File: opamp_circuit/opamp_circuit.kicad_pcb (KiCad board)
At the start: 2 copper layers, 49 parts, among them J1 INP, J2 INM, J3 Vout, J4 VDD, J5 VSS, J6 Vref, J7 Vref_out, J8 GND, U1 OPA846xDBV, U2 OPA846xDBV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

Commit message: Version Vicente before advices
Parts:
- moved C22 89.8 mm to (62.7, 67.9)
- moved C20 89.6 mm to (62.7, 71.7)
- moved C21 88.7 mm to (62.7, 70.2)
- moved J3 87.7 mm to (75.2, 63.0)
- moved R9 86.6 mm to (66.2, 63.1)
- moved U3 85.1 mm to (57.5, 63.7)
- moved C27 79.9 mm to (55.6, 71.8)
- moved Rg1 79.6 mm to (51.3, 63.8)
- moved C26 79.5 mm to (55.6, 70.4)
- moved C23 79.3 mm to (60.4, 54.9)
- moved C25 78.6 mm to (61.2, 59.1)
- moved C24 78.3 mm to (60.6, 56.8)
- moved R6 77.4 mm to (55.6, 68.7), turned to 180 degrees
- moved R5 72.4 mm to (53.0, 69.5), turned to 90 degrees
- moved R8 61.8 mm to (62.7, 53.1)
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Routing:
- net VSS: track 0.00 -> 98.6 mm, vias 0 -> 2
- net VDD: track 0.00 -> 56.4 mm, vias 0 -> 2
- net Vref: track 0.00 -> 45.7 mm
- net Net-(C2-Pad2): track 0.00 -> 19.0 mm
- net Net-(C11-Pad2): track 0.00 -> 18.4 mm
- net Net-(C2-Pad1): track 0.00 -> 18.3 mm
- net Net-(C11-Pad1): track 0.00 -> 17.9 mm
- net Net-(R7-Pad2): track 0.00 -> 15.7 mm
- net Net-(R8-Pad2): track 0.00 -> 13.6 mm
- net Net-(JP1-Pad2): track 0.00 -> 9.66 mm
- net Net-(C26-Pad1): track 0.00 -> 8.20 mm
- net Net-(J3-Pad1): track 0.00 -> 6.36 mm
- net Net-(JP2-Pad2): track 0.00 -> 6.28 mm
- net Net-(C12-Pad1): track 0.00 -> 4.87 mm
- net Net-(C10-Pad1): track 0.00 -> 4.36 mm
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- added copper zone on B.Cu, net GND
- added copper zone on F.Cu, net GND

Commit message: Adjustements after Yassine's advices
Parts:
- moved R4 38.7 mm to (76.4, 48.4), turned to -90 degrees
- moved C13 37.5 mm to (77.6, 51.4), turned to -90 degrees
- moved C19 37.2 mm to (75.1, 48.5), turned to 90 degrees
- moved C14 35.5 mm to (76.1, 51.7), turned to -90 degrees
- moved C12 35.5 mm to (73.5, 48.5), turned to 90 degrees
- moved J3 34.8 mm to (42.1, 73.6)
- moved R1 33.9 mm to (36.3, 51.3), turned to -90 degrees
- moved C15 32.3 mm to (73.9, 52.6), turned to -90 degrees
- moved J1 32.0 mm to (36.3, 43.8)
- moved C2 31.7 mm to (38.2, 51.4), turned to -90 degrees
- moved U2 30.4 mm to (70.4, 50.5), turned to 180 degrees
- moved J2 28.2 mm to (58.8, 43.4)
- moved C7 27.3 mm to (40.5, 53.5), turned to 90 degrees
- moved C8 26.0 mm to (41.9, 53.3), turned to 90 degrees
- moved C3 25.6 mm to (51.1, 48.1), turned to 90 degrees
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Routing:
- net Vref_out: track 0.00 -> 45.0 mm, vias 0 -> 1
- net VDD: track 56.4 -> 77.0 mm, vias 2 -> 3
- net Vref: track 45.7 -> 63.7 mm
- net VSS: track 98.6 -> 87.4 mm, vias 2 -> 4
- net Net-(J3-Pad1): track 6.36 -> 14.3 mm
- net Net-(C26-Pad1): track 8.20 -> 12.7 mm
- net Net-(JP1-Pad2): track 9.66 -> 5.76 mm
- net Net-(JP2-Pad2): track 6.28 -> 3.79 mm
- net Net-(C2-Pad2): track 19.0 -> 17.1 mm

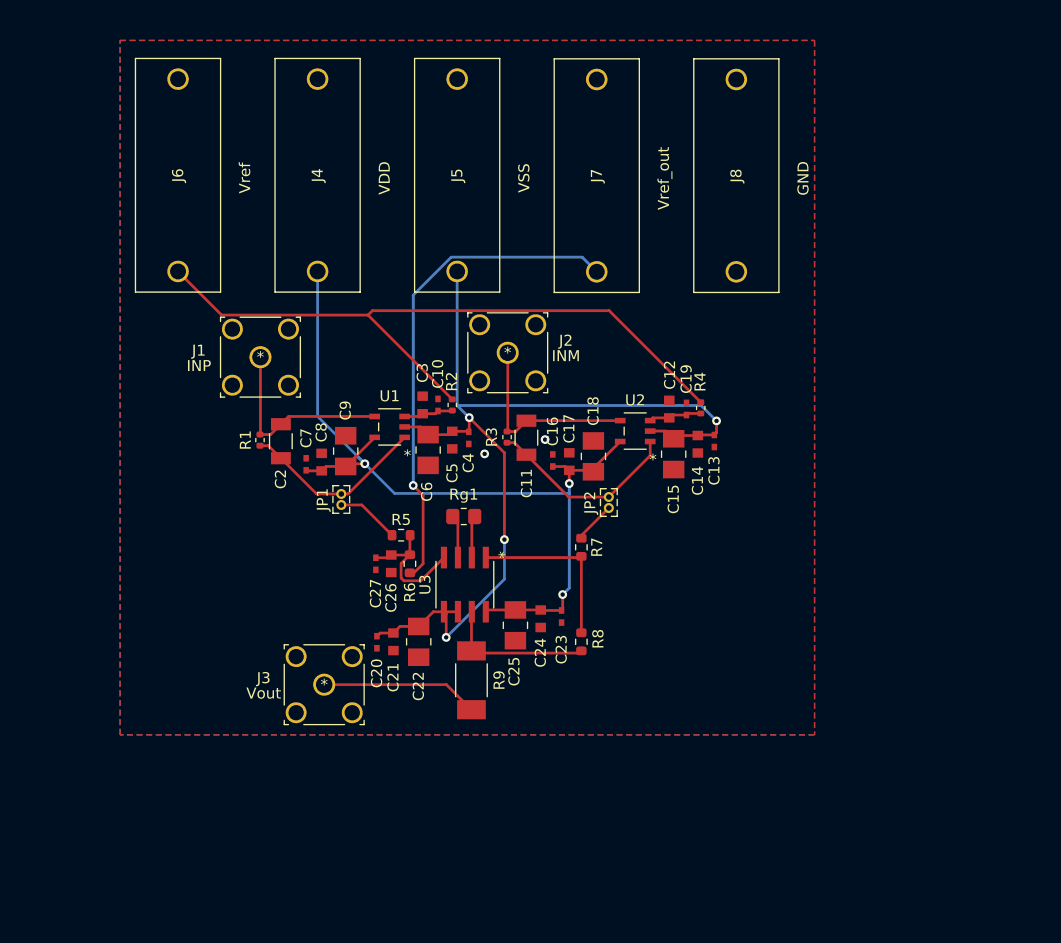
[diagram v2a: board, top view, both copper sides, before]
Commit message: First version pcb. Need to: change cp to same dims and check constraints from the manufacturer
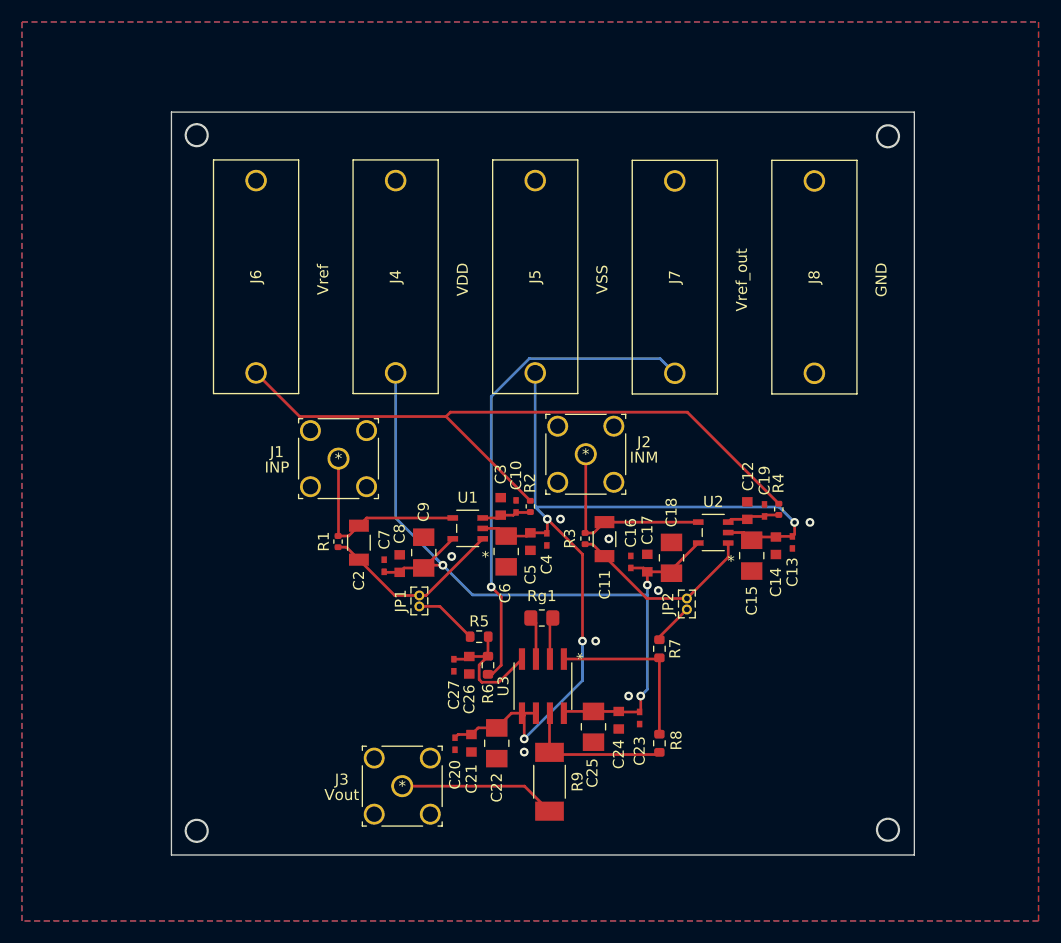
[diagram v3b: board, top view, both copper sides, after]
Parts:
- moved C14 11.6 mm to (83.2, 61.0)
- moved C18 11.6 mm to (73.7, 62.1)
- moved C19 11.6 mm to (82.2, 57.7)
- moved C20 11.6 mm to (54.0, 79.0)
- moved C21 11.6 mm to (55.5, 78.9)
- moved C23 11.6 mm to (70.8, 76.6)
- moved C24 11.6 mm to (68.9, 76.8)
- moved C25 11.6 mm to (66.6, 77.4)
- moved C7 11.6 mm to (47.6, 62.8)
- moved C8 11.6 mm to (49.0, 62.6)
- moved C9 11.6 mm to (51.2, 61.6)
- moved J1 11.6 mm to (43.4, 53.0)
- moved J2 11.6 mm to (65.9, 52.6)
- moved R8 11.6 mm to (72.6, 78.9)
- moved Rg1 11.6 mm to (61.9, 67.5)
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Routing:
- net GND: vias 2 -> 8
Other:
- board outline added: 67.6 x 67.6 mm

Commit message: Better placement and uniform capa, redesign adapting to the instrumentation opamp
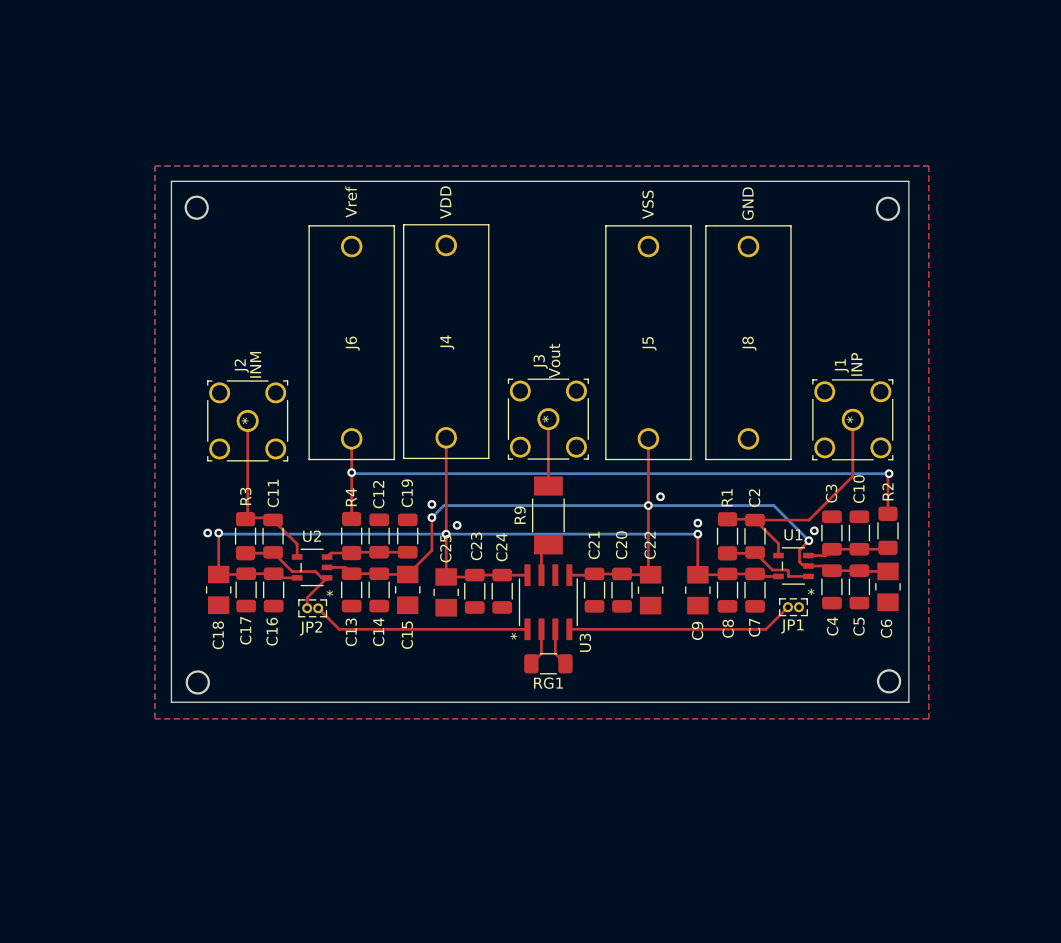
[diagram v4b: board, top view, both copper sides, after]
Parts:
- removed C26: 10nF, created_lib:06035C103JAT2A
- removed C27: 100pF, created_lib:CL05C101JB5NNNC
- removed J7: Vref_out, created_lib:973582101
- removed R5, R7: 200Ω, Resistor_SMD:R_0603_1608Metric
- removed R6, R8: 402Ω, Resistor_SMD:R_0603_1608Metric
- C10, C13, C16, C19, C20, C23, C4, C7: footprint created_lib:CL05C101JB5NNNC -> Capacitor_SMD:C_1206_3216Metric
- C11, C2: footprint created_lib:CC1206JRNPO9BN102 -> Capacitor_SMD:C_1206_3216Metric
- C12, C14, C17, C21, C24, C3, C5, C8: footprint created_lib:06035C103JAT2A -> Capacitor_SMD:C_1206_3216Metric
- R1, R2, R3, R4: footprint Resistor_SMD:R_0402_1005Metric -> Resistor_SMD:R_1206_3216Metric_Pad1.30x1.75mm_HandSolder
- RG1: renamed from Rg1; footprint Resistor_SMD:R_0805_2012Metric_Pad1.20x1.40mm_HandSolder -> Resistor_SMD:R_1206_3216Metric_Pad1.30x1.75mm_HandSolder
- moved J1 46.9 mm to (90.2, 49.5), turned to -90 degrees
- moved C18 41.3 mm to (32.5, 65.0), turned to -90 degrees
- moved C13 40.3 mm to (44.6, 65.0)
- moved R4 38.9 mm to (44.6, 60.1)
- moved U2 36.6 mm to (41.0, 62.9)
- moved C17 36.6 mm to (35.0, 65.0), turned to -90 degrees
- moved C14 36.3 mm to (47.1, 65.0)
- moved C2 36.0 mm to (81.3, 60.1)
- moved J3 35.9 mm to (62.5, 49.4), turned to 90 degrees
- moved R1 35.4 mm to (78.8, 60.1)
- moved C6 34.9 mm to (93.4, 64.7)
- moved JP2 34.6 mm to (40.6, 66.7), turned to 0 degrees
- moved JP1 34.6 mm to (85.3, 66.6), turned to 180 degrees
- moved C7 33.8 mm to (81.3, 65.0), turned to -90 degrees
- moved C12 33.6 mm to (47.1, 60.1)
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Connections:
- U3 pad 1: Net-(R7-Pad2) -> Net-(JP2-Pad2)
- U3 pad 4: Net-(C26-Pad1) -> Net-(JP1-Pad2)
- U3 pad 6: VSS -> GND
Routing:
- net Vref_out: track 45.0 -> 0.00 mm, vias 1 -> 0
- net Net-(JP2-Pad2): track 3.79 -> 19.8 mm
- net Net-(R7-Pad2): track 15.7 -> 0.00 mm
- net Net-(JP1-Pad2): track 5.76 -> 20.7 mm
- net Net-(C26-Pad1): track 12.7 -> 0.00 mm
- net Net-(R9-Pad1): track 13.7 -> 3.02 mm
- net VDD: track 77.0 -> 86.0 mm
- net Net-(C2-Pad2): track 17.1 -> 8.59 mm
- net Net-(J3-Pad1): track 14.3 -> 6.09 mm
- net VSS: track 87.4 -> 80.4 mm, vias 4 -> 3
- net Net-(C11-Pad2): track 17.9 -> 11.9 mm
- net Net-(C2-Pad1): track 18.4 -> 22.3 mm
- net Vref: track 63.7 -> 59.9 mm, vias 0 -> 2
- net Net-(C10-Pad1): track 4.56 -> 7.53 mm
- net Net-(C12-Pad1): track 4.87 -> 7.52 mm
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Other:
- board size 67.6 x 67.6 mm -> 67.1 x 47.4 mm

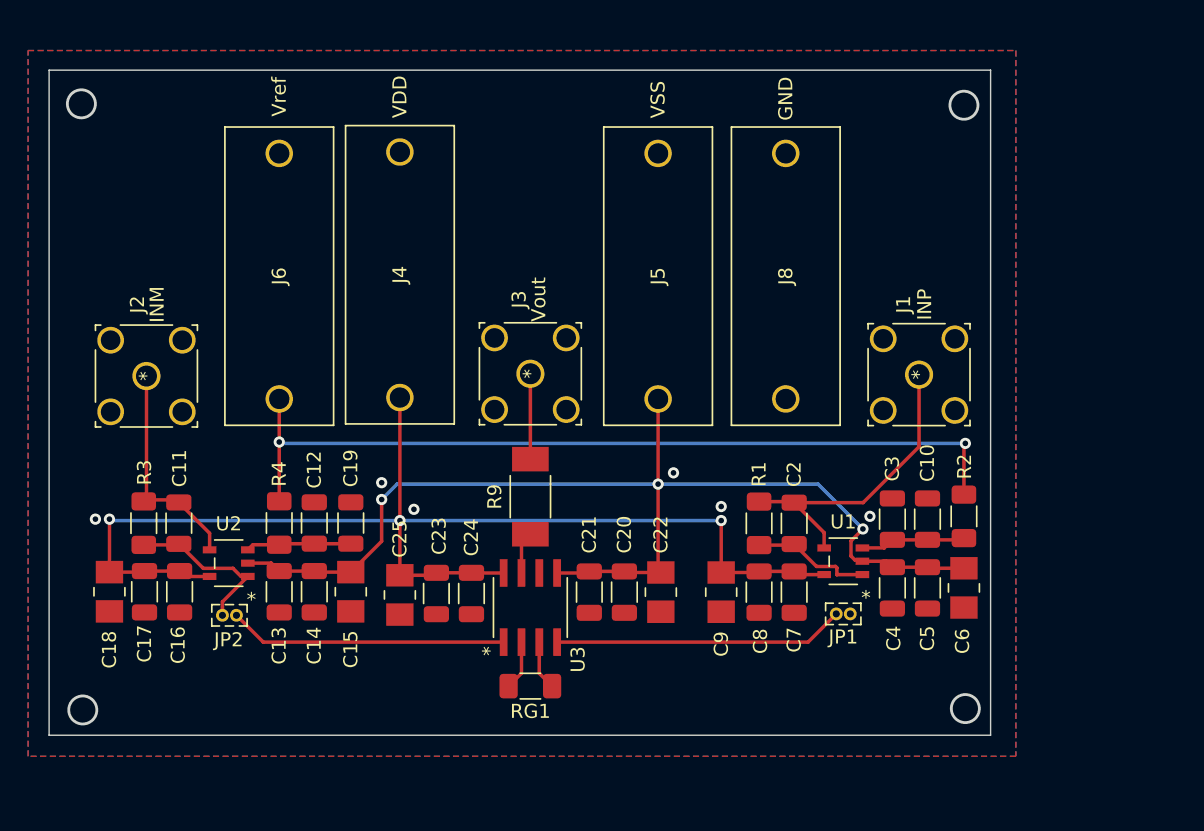
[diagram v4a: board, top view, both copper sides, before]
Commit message: Renamed capa
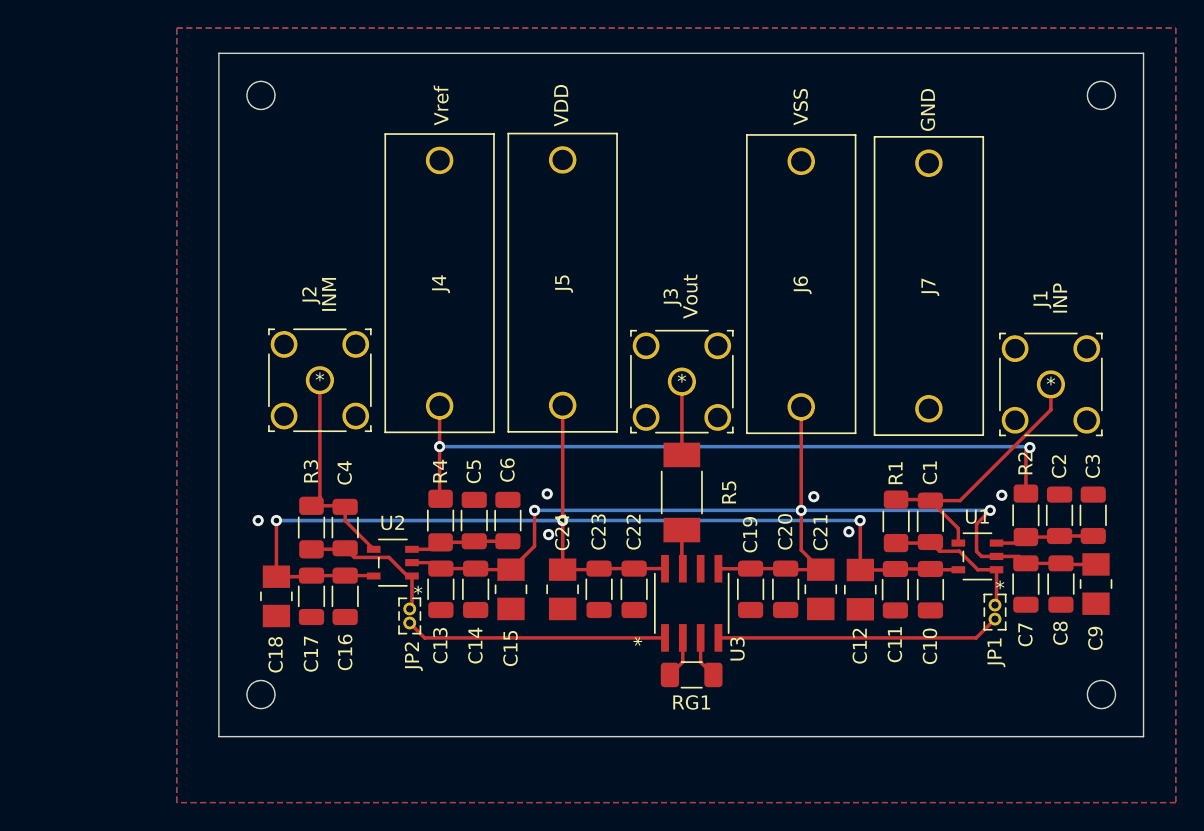
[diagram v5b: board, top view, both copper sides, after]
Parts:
- removed C25: 10uF, created_lib:C1206X106J4RACAUTO
- removed J8: GND, created_lib:973582101
- removed R9: 50Ω, created_lib:WSC251550R00FEA
- added C1: 1pF, Capacitor_SMD:C_1206_3216Metric, F.Cu at (91.0, 60.0)
- added J7: GND, created_lib:973582101, F.Cu at (90.9, 34.4)
- added R5: 50Ω, created_lib:WSC251550R00FEA, F.Cu at (73.3, 57.9)
- C11, C2: value 1pF -> 10nF
- C12, C21, C24: value 10nF -> 10uF; footprint Capacitor_SMD:C_1206_3216Metric -> created_lib:C1206X106J4RACAUTO
- C20, C23: value 100pF -> 10nF
- C22, C6: value 10uF -> 100pF; footprint created_lib:C1206X106J4RACAUTO -> Capacitor_SMD:C_1206_3216Metric
- C3: value 10nF -> 100pF
- C4: value 100pF -> 1pF
- J4: value VDD -> Vref
- J5: value VSS -> VDD
- J6: value Vref -> VSS
- moved C11 51.3 mm to (88.5, 64.8)
- moved C4 39.2 mm to (49.3, 60.4)
- moved C12 39.2 mm to (86.0, 64.8), turned to -90 degrees
- moved J6 37.2 mm to (81.8, 34.3)
- moved C6 32.9 mm to (60.9, 59.9), turned to 90 degrees
- moved C5 32.7 mm to (58.5, 59.9), turned to 90 degrees
- moved C19 28.9 mm to (78.2, 64.8), turned to -90 degrees
- moved C9 26.7 mm to (102.8, 64.4)
- moved C8 21.5 mm to (100.3, 64.4)
- moved C2 18.9 mm to (100.2, 59.5), turned to 90 degrees
- moved C7 16.5 mm to (97.8, 64.4)
- moved C21 16.5 mm to (83.2, 64.8)
- moved C3 14.3 mm to (102.6, 59.5)
- moved JP2 13.4 mm to (53.9, 66.2), turned to -90 degrees
- moved J2 12.4 mm to (47.5, 49.9), turned to 180 degrees
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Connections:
- C10 pad 1: Net-(C10-Pad1) -> VDD
- C11 pad 1: Net-(C11-Pad1) -> VDD
- C11 pad 2: Net-(C11-Pad2) -> GND
- C12 pad 1: Net-(C12-Pad1) -> VDD
- C19 pad 1: Net-(C12-Pad1) -> VSS
- C2 pad 1: Net-(C2-Pad1) -> Net-(C3-Pad1)
- C2 pad 2: Net-(C2-Pad2) -> GND
- C22 pad 1: VSS -> VDD
- C3 pad 1: Net-(C10-Pad1) -> Net-(C3-Pad1)
- C4 pad 1: VSS -> Net-(C4-Pad1)
- C4 pad 2: GND -> Net-(C4-Pad2)
- C5 pad 1: VSS -> Net-(C5-Pad1)
- C6 pad 1: VSS -> Net-(C5-Pad1)
- C7 pad 1: VDD -> VSS
- C8 pad 1: VDD -> VSS
- C9 pad 1: VDD -> VSS
- J1 pad 1: Net-(C2-Pad1) -> Net-(C1-Pad1)
- J2 pad 1: Net-(C11-Pad1) -> Net-(C4-Pad1)
- J4 pad 1: VDD -> Vref
- J5 pad 1: VSS -> VDD
- J6 pad 1: Vref -> VSS
- JP1 pad 1: Net-(C2-Pad2) -> Net-(C1-Pad2)
- JP2 pad 1: Net-(C11-Pad2) -> Net-(C4-Pad2)
- R1 pad 1: Net-(C2-Pad1) -> Net-(C1-Pad1)
- R1 pad 2: Net-(C2-Pad2) -> Net-(C1-Pad2)
- R2 pad 2: Net-(C10-Pad1) -> Net-(C3-Pad1)
- R3 pad 1: Net-(C11-Pad1) -> Net-(C4-Pad1)
- R3 pad 2: Net-(C11-Pad2) -> Net-(C4-Pad2)
- R4 pad 2: Net-(C12-Pad1) -> Net-(C5-Pad1)
- U1 pad 1: Net-(C2-Pad2) -> Net-(C1-Pad2)
- U1 pad 3: Net-(C10-Pad1) -> Net-(C3-Pad1)
- U1 pad 4: Net-(C2-Pad1) -> Net-(C1-Pad1)
- U2 pad 1: Net-(C11-Pad2) -> Net-(C4-Pad2)
- U2 pad 3: Net-(C12-Pad1) -> Net-(C5-Pad1)
- U2 pad 4: Net-(C11-Pad1) -> Net-(C4-Pad1)
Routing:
- net Net-(C2-Pad1): track 22.3 -> 0.00 mm
- net Net-(C1-Pad1): track 0.00 -> 19.4 mm
- net Net-(C11-Pad1): track 15.9 -> 0.00 mm
- net Net-(C4-Pad1): track 0.00 -> 15.5 mm
- net Net-(C11-Pad2): track 11.9 -> 0.00 mm
- net Net-(C1-Pad2): track 0.00 -> 10.6 mm
- net Net-(C4-Pad2): track 0.00 -> 10.4 mm
- net Net-(C2-Pad2): track 8.59 -> 0.00 mm
- net Vref: track 59.9 -> 52.1 mm
- net Net-(C10-Pad1): track 7.53 -> 0.00 mm
- net Net-(C12-Pad1): track 7.52 -> 0.00 mm
- net Net-(C3-Pad1): track 0.00 -> 7.10 mm
- net Net-(C5-Pad1): track 0.00 -> 7.08 mm
- net VDD: track 86.0 -> 82.2 mm
- net VSS: track 80.4 -> 77.4 mm
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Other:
- board size 67.1 x 47.4 mm -> 65.9 x 48.7 mm
